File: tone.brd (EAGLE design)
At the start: 29.2 x 97.5 mm, 42 parts, among them IC1 TL074D

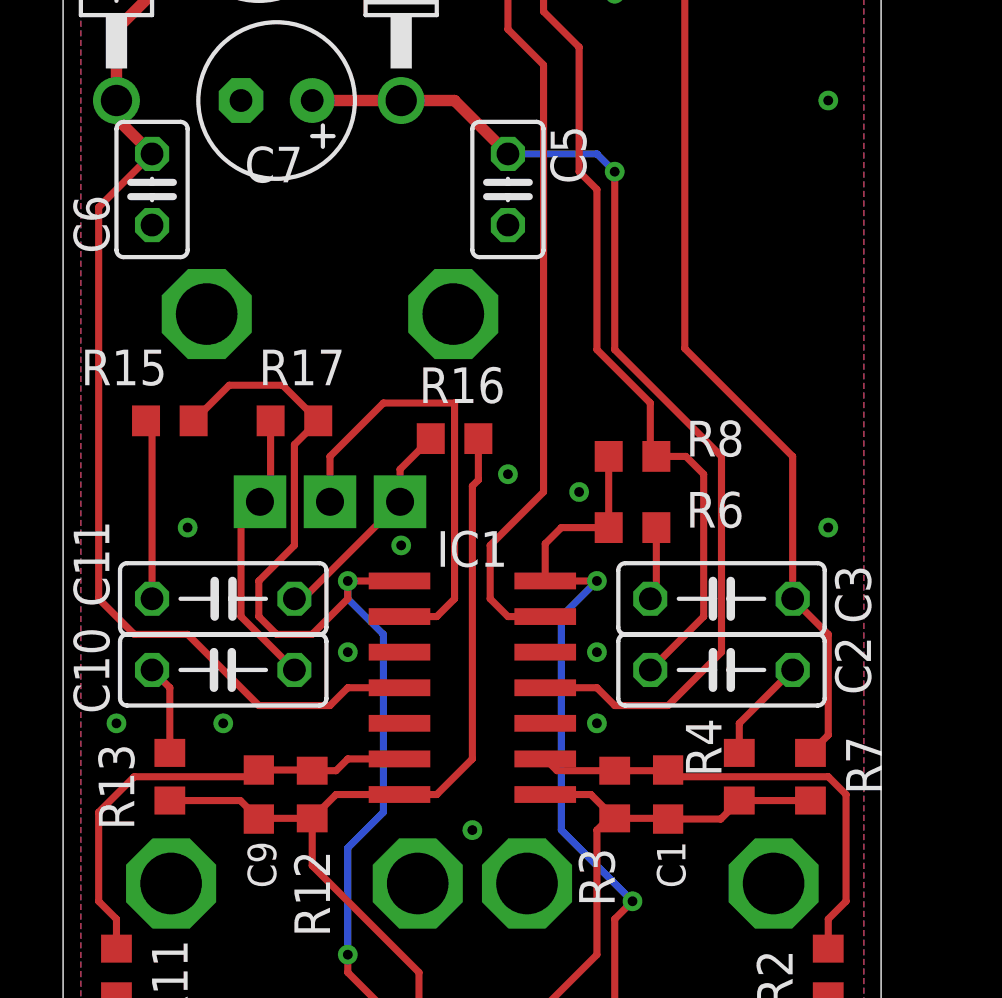
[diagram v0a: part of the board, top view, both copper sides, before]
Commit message: Rotated & rerouted a few resistors. Simpler to solder board if all are in one direction. Added type label & pin 1 indicator for IC1.
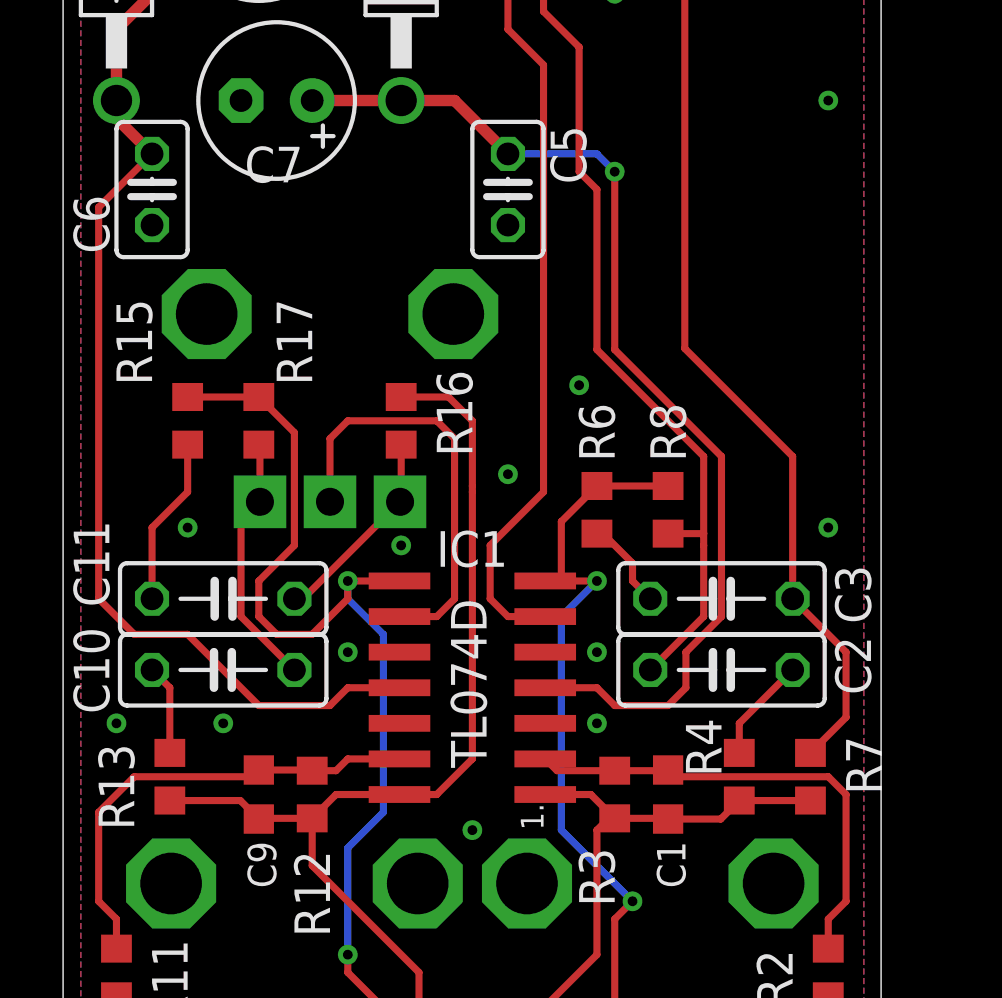
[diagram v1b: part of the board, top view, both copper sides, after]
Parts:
- moved R8 2.29 mm to (22.2, 59.1), turned to 90 degrees
- moved R16 2.01 mm to (12.7, 62.2), turned to 270 degrees
- moved R6 1.42 mm to (19.7, 59.1), turned to 90 degrees
- moved R17 1.27 mm to (7.62, 62.2), turned to 90 degrees
- moved R15 0.63 mm to (5.08, 62.2), turned to 90 degrees
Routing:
- net N$20: track 52.3 -> 55.8 mm
- net N$25: track 70.4 -> 68.4 mm
- net N$22: track 10.1 -> 9.13 mm
- net N$31: track 16.1 -> 15.2 mm
- net N$23: track 7.91 -> 7.26 mm
- net N$4: track 30.2 -> 30.8 mm
- net N$6: track 2.63 -> 3.24 mm
- net N$5: track 31.7 -> 32.2 mm
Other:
- board text added: "1."
